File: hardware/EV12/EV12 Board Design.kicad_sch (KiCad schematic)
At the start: 132 parts, among them CN2 Conn_05x02_Female, CN3 Conn_01x06_Female, CN4 Conn_01x06_Female, CN5 Conn_02x05_Male, CN6 Conn_02x05_Male, CN7 Conn_02x05_Male, J1 Conn_01x02_Socket, J10 Conn_01x08_Socket, J2 AudioJack1, J3 Conn_01x06_Socket, J9 USB_C_Receptacle, Q1 SS8050, Q2 SS8050, SW1 TS-1037-A11B3-D2, SW3 TS-1037-A11B3-D2, SW4 SW_Push, SW5 SW_Push, SW6 SW_SPDT, U1 STM32F405RGTx, U11 ESP32-S3-WROOM-1-N8R2, U13 BM14B(0.8)-24DS-0.4V(53), U2 BQ21040DBV, U3 CH340C, U4 USBLC6-2P6, U5 M24C02-RMN6TP, U6 WM8960CGEFL/RV, U7 TPS63060, U8 STM32F072CBTx, Y1 Crystal_GND24

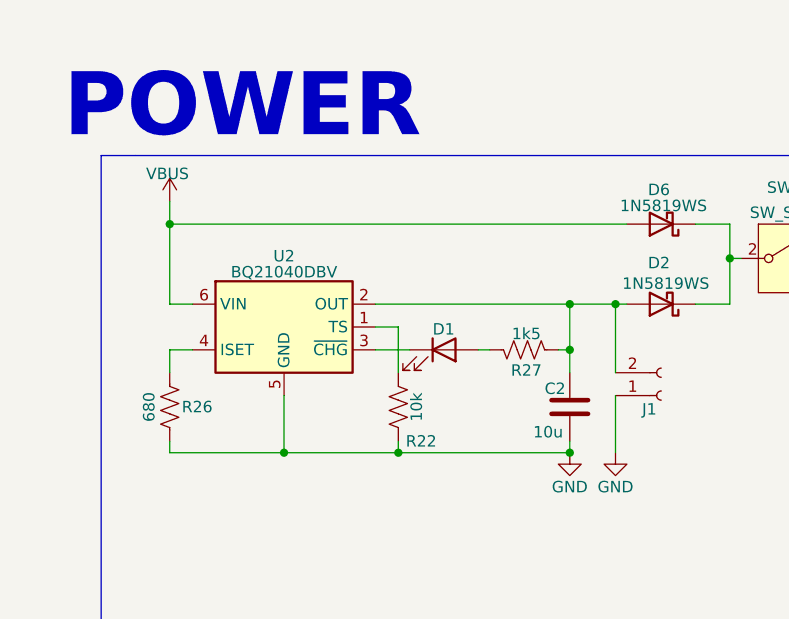
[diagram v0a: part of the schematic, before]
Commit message: Added missing capacitor to BQ21040DVR battery charger
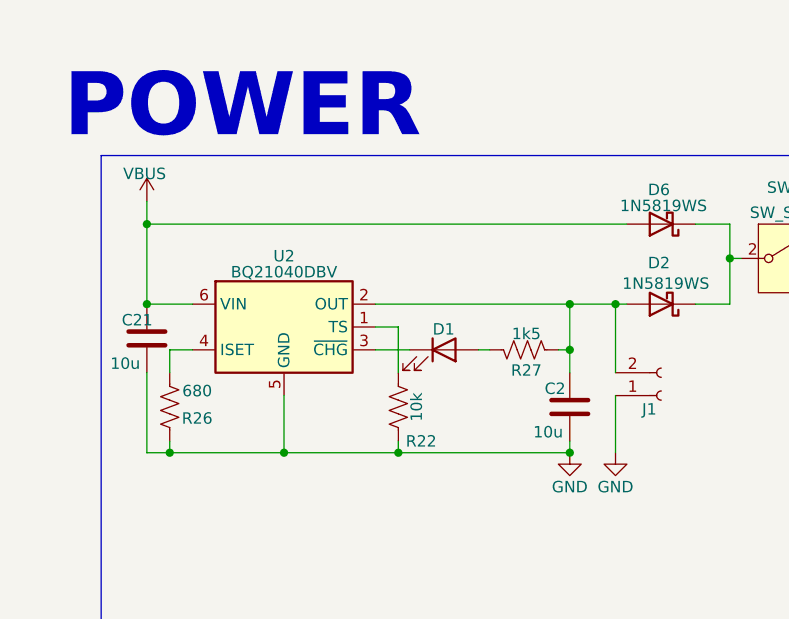
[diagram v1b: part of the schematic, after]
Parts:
- added C21: 10u, Capacitor_SMD:C_0402_1005Metric, symbol Device:C
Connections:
- net GND: now also C21.2
- net VBUS: now also C21.1
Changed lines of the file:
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@@
 	)
 	(junction
+		(at 33.02 311.15)
+		(diameter 0)
+		(color 0 0 0 0)
+	)
+	(junction
 		(at 265.43 351.79)
 		(diameter 0)
@@
 	)
 	(junction
+		(at 35.56 327.66)
+		(diameter 0)
+		(color 0 0 0 0)
+	)
+	(junction
 		(at 405.13 161.29)
 		(diameter 0)
@@
 	)
 	(junction
+		(at 33.02 302.26)
+		(diameter 0)
+		(color 0 0 0 0)
+	)
+	(junction
 		(at 196.85 351.79)
 		(diameter 0)
@@
 		(color 0 0 0 0)
 	)
-	(junction
-		(at 35.56 302.26)
-		(diameter 0)
-		(color 0 0 0 0)
-	)
 	(no_connect
 		(at 196.85 127)
@@
 		)
 	)
+	(wire
+		(pts
+			(xy 33.02 302.26) (xy 86.36 302.26)
+		)
+		(stroke
+			(width 0)
+			(type default)
+		)
+	)
 	(polyline
 		(pts
@@
 	(wire
 		(pts
+			(xy 35.56 327.66) (xy 48.26 327.66)
+		)
+		(stroke
+			(width 0)
+			(type default)
+		)
+	)
+	(wire
+		(pts
 			(xy 80.01 311.15) (xy 80.01 316.23)
 		)
@@
 	(wire
 		(pts
-			(xy 35.56 311.15) (xy 38.1 311.15)
+			(xy 33.02 311.15) (xy 38.1 311.15)
 		)
 		(stroke
@@
 	(wire
 		(pts
-			(xy 35.56 327.66) (xy 48.26 327.66)
-		)
-		(stroke
-			(width 0)
-			(type default)
-		)
-	)
-	(wire
-		(pts
 			(xy 403.86 290.83) (xy 403.86 293.37)
 		)
@@
 	(wire
 		(pts
+			(xy 33.02 327.66) (xy 35.56 327.66)
+		)
+		(stroke
+			(width 0)
+			(type default)
+		)
+	)
+	(wire
+		(pts
 			(xy 129.54 128.27) (xy 140.97 128.27)
 		)
@@
 		)
 	)
+	(wire
+		(pts
+			(xy 33.02 318.77) (xy 33.02 327.66)
+		)
+		(stroke
+			(width 0)
+			(type default)
+		)
+	)
 	(polyline
 		(pts
@@
 	(wire
 		(pts
-			(xy 35.56 302.26) (xy 35.56 311.15)
+			(xy 33.02 302.26) (xy 33.02 311.15)
 		)
 		(stroke
@@
 	(wire
 		(pts
-			(xy 35.56 302.26) (xy 86.36 302.26)
-		)
-		(stroke
-			(width 0)
-			(type default)
-		)
-	)
-	(wire
-		(pts
 			(xy 293.37 288.29) (xy 293.37 293.37)
 		)
@@
 	(wire
 		(pts
-			(xy 35.56 299.72) (xy 35.56 302.26)
+			(xy 33.02 299.72) (xy 33.02 302.26)
 		)
 		(stroke
@@
 		(dnp no)
 		(property "Reference" "R26"
-			(at 38.608 322.58 0)
+			(at 38.608 323.85 0)
 			(effects
 				(font
@@
 		)
 		(property "Value" "680"
-			(at 33.274 322.58 90)
+			(at 38.608 320.802 0)
 			(effects
 				(font
@@
 	)
 	(symbol
+		(lib_id "Device:C")
+		(at 33.02 314.96 0)
+		(unit 1)
+		(exclude_from_sim no)
+		(in_bom yes)
+		(on_board yes)
+		(dnp no)
+		(property "Reference" "C21"
+			(at 30.226 312.928 0)
+			(effects
+				(font
+					(size 1.27 1.27)
+				)
+				(justify left)
+			)
+		)
+		(property "Value" "10u"
+			(at 28.956 317.754 0)
+			(effects
+				(font
+					(size 1.27 1.27)
+				)
+				(justify left)
+			)
+		)
+		(property "Footprint" "Capacitor_SMD:C_0402_1005Metric"
+			(at 33.9852 318.77 0)
+			(effects
+				(font
+					(size 1.27 1.27)
+				)
+				(hide yes)
+			)
+		)
+		(property "Datasheet" "~"
+			(at 33.02 314.96 0)
+			(effects
+				(font
+					(size 1.27 1.27)
+				)
+				(hide yes)
+			)
+		)
+		(property "Description" "Unpolarized capacitor"
+			(at 33.02 314.96 0)
+			(effects
+				(font
+					(size 1.27 1.27)
+				)
+				(hide yes)
+			)
+		)
+		(property "JLCPCB Part #" "C307415"
+			(at 33.02 314.96 0)
+			(effects
+				(font
+					(size 1.27 1.27)
+				)
+				(hide yes)
+			)
+		)
+		(pin "1"
+		)
+		(pin "2"
+		)
+		(instances
+			(project "EV12 Board Design"
+				(path "/bd865368-262b-4f76-b7a6-1673c2cb0f8c"
+					(reference "C21")
+					(unit 1)
+				)
+			)
+		)
+	)
+	(symbol
 		(lib_id "Device:R_US")
 		(at 109.22 331.47 180)
@@
 	(symbol
 		(lib_id "power:VBUS")
-		(at 35.56 299.72 0)
+		(at 33.02 299.72 0)
 		(unit 1)
 		(exclude_from_sim no)
@@
 		(dnp no)
 		(property "Reference" "#PWR03"
-			(at 35.56 303.53 0)
+			(at 33.02 303.53 0)
 			(effects
 				(font
@@
 		)
 		(property "Value" "VBUS"
-			(at 35.306 296.672 0)
+			(at 32.766 296.672 0)
 			(effects
 				(font
@@
 		)
 		(property "Footprint" ""
-			(at 35.56 299.72 0)
+			(at 33.02 299.72 0)
 			(effects
 				(font
@@
 		)
 		(property "Datasheet" ""
-			(at 35.56 299.72 0)
+			(at 33.02 299.72 0)
 			(effects
 				(font
@@
 		)
 		(property "Description" "Power symbol creates a global label with name \"VBUS\""
-			(at 35.56 299.72 0)
+			(at 33.02 299.72 0)
 			(effects
 				(font

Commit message: Moved keyboard conn, eeprom, and battery connector. Added diodes
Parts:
- added D10, D11, D12, D13, D14, D15, D8, D9: 1N5819WS, Diode_SMD:D_SOD-323, symbol Device:D_Schottky
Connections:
- net NET_BOOT: now also D12.1 (K); no longer U8.41 (PB5)
- net NET_DTR: now also D11.2 (A); no longer Q1.2 (E), R44.1
- net NET_NRST: now also D13.1 (K); no longer U8.40 (PB4)
- net NET_RTS: now also D10.2 (A); no longer Q2.2 (E), R43.1
- net UI_BOOT0: now also D14.1 (K), D9.1 (K); no longer CN4.5 (Pin_5), U8.39 (PB3)
- net UI_NRST: now also D15.1 (K), D8.1 (K); no longer CN4.4 (Pin_4), U8.38 (PA15)
- new net: D12.2 (A), U8.38 (PA15)
- new net: CN4.4 (Pin_4), D15.2 (A)
- new net: CN4.5 (Pin_5), D14.2 (A)
- new net: D13.2 (A), U8.39 (PB3)
- new net: D8.2 (A), U8.40 (PB4)
- new net: D9.2 (A), U8.41 (PB5)
- new net: D11.1 (K), Q1.2 (E), R44.1
- new net: D10.1 (K), Q2.2 (E), R43.1
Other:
- note added: "UI ST-LINK - 2MM R"
- note removed: "MAIN ST-LINK - 2MM R"
- moved on the sheet: CN4, Q1, Q2, R4, R43, R44

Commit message: Removed diodes and auto reset circuit
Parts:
- removed D10, D11, D12, D13, D14, D15, D8, D9: 1N5819WS, Diode_SMD:D_SOD-323, symbol Device:D_Schottky
- removed Q1, Q2: SS8050, Package_TO_SOT_SMD:SOT-23, symbol Transistor_BJT:SS8050
- removed R43, R44: 10k, Resistor_SMD:R_0402_1005Metric, symbol Device:R_US
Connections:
- net NET_DTR is gone; now on net NET_BOOT: J3.2 (Pin_2)
- net NET_RTS is gone; now on net NET_NRST: J3.5 (Pin_5)
- net NET_BOOT: now also U8.41 (PB5)
- net NET_NRST: now also U8.40 (PB4)
- net UI_BOOT0: now also CN4.5 (Pin_5), U8.38 (PA15)
- net UI_NRST: now also CN4.4 (Pin_4), U8.39 (PB3)
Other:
- note removed: "NET AUTO RESET"

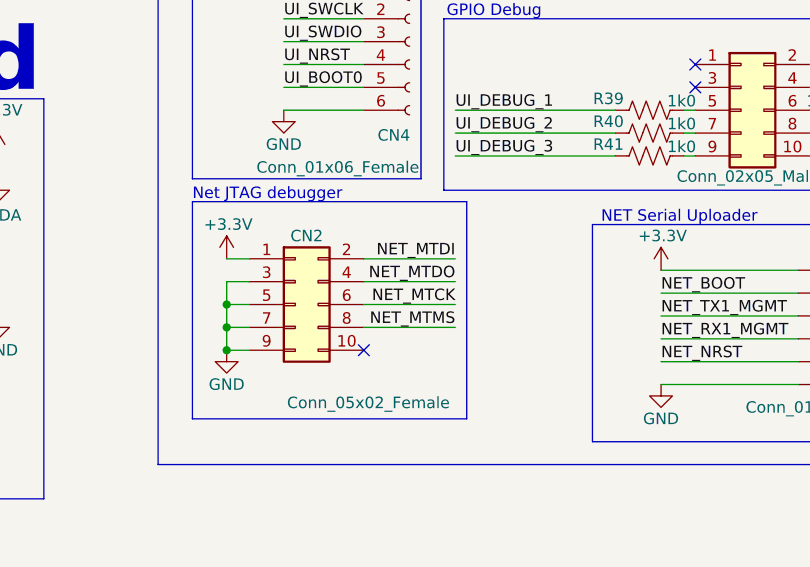
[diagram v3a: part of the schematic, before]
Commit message: Added some design rules, updated track widths to be between 5 to 15mils except for long power lines
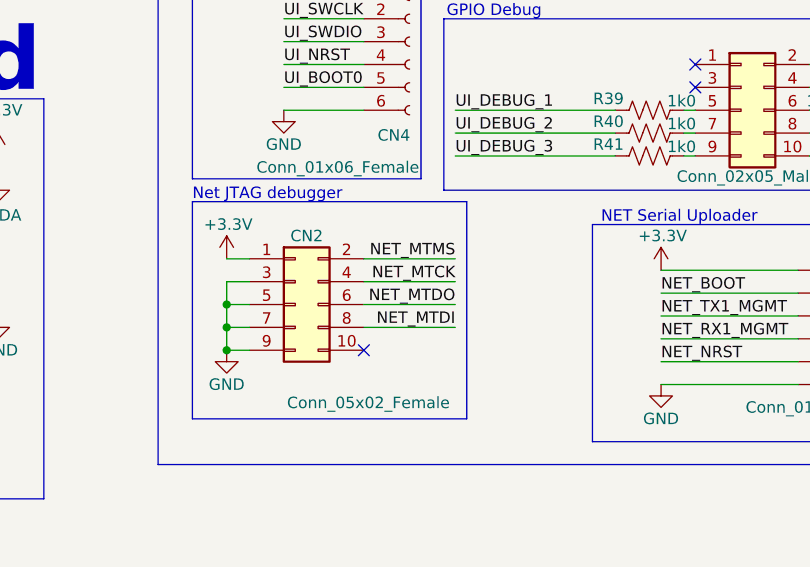
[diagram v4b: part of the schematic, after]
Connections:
- net NET_MTCK: now also CN2.4 (Pin_4); no longer CN2.6 (Pin_6)
- net NET_MTDI: now also CN2.8 (Pin_8); no longer CN2.2 (Pin_2)
- net NET_MTDO: now also CN2.6 (Pin_6); no longer CN2.4 (Pin_4)
- net NET_MTMS: now also CN2.2 (Pin_2); no longer CN2.8 (Pin_8)
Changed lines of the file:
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@@
+		)
+	)
+	(label "NET_MTDO"
+		(at 429.26 288.29 180)
+		(fields_autoplaced yes)
+		(effects
+			(font
+				(size 1.27 1.27)
+			)
+			(justify right bottom)
 		)
 	)
@@
 		)
 	)
-	(label "NET_MTDI"
-		(at 429.26 283.21 180)
-		(fields_autoplaced yes)
-		(effects
-			(font
-				(size 1.27 1.27)
-			)
-			(justify right bottom)
-		)
-	)
 	(label "NET_NRST"
 		(at 181.61 96.52 0)
@@
 		)
 	)
-	(label "NET_MTDO"
-		(at 429.26 285.75 180)
-		(fields_autoplaced yes)
-		(effects
-			(font
-				(size 1.27 1.27)
-			)
-			(justify right bottom)
-		)
-	)
 	(label "DISP_RST"
 		(at 314.96 223.52 0)
@@
 		)
 	)
-	(label "NET_MTCK"
-		(at 429.26 288.29 180)
-		(fields_autoplaced yes)
-		(effects
-			(font
-				(size 1.27 1.27)
-			)
-			(justify right bottom)
-		)
-	)
 	(label "NET_RX1_MGMT"
 		(at 452.12 292.1 0)
@@
 		)
 	)
+	(label "NET_MTDI"
+		(at 429.26 290.83 180)
+		(fields_autoplaced yes)
+		(effects
+			(font
+				(size 1.27 1.27)
+			)
+			(justify right bottom)
+		)
+	)
 	(label "UI_SCL"
 		(at 214.63 214.63 0)
@@
 		)
 	)
-	(label "NET_MTMS"
-		(at 429.26 290.83 180)
-		(fields_autoplaced yes)
-		(effects
-			(font
-				(size 1.27 1.27)
-			)
-			(justify right bottom)
-		)
-	)
 	(label "UI_SDA"
 		(at 287.02 283.21 0)
@@
 		)
 	)
+	(label "NET_MTCK"
+		(at 429.26 285.75 180)
+		(fields_autoplaced yes)
+		(effects
+			(font
+				(size 1.27 1.27)
+			)
+			(justify right bottom)
+		)
+	)
 	(label "I2S_DACDAT"
 		(at 485.14 247.65 180)
@@
 		(fields_autoplaced yes)
 		(effects
+			(font
+				(size 1.27 1.27)
+			)
+			(justify right bottom)
+		)
+	)
+	(label "NET_MTMS"
+		(at 429.26 283.21 180)
+		(fields_autoplaced yes)
+		(effects

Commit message: Finish ev12 design
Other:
- company: CISCO SYSTEMS -> CISCO SYSTEMS INC
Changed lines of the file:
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@@
 		(title "EV12 FINN BERG & BRETT REGNIER")
 		(date "2024/07/19")
-		(company "CISCO SYSTEMS")
+		(company "CISCO SYSTEMS INC")
 	)
 	(junction

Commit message: Added missing jlcpcb part number
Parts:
- R42: JLCPCB Part # (none) -> C111027
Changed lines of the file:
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@@
 			)
 		)
-		(property "JLCPCB Part #" ""
+		(property "JLCPCB Part #" "C111027"
 			(at 116.84 322.58 0)
 			(effects

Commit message: Replaced side buttons, switched Cap, switched to new connectors
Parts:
- SW1, SW3: footprint Hactar_Footprints:KEY-SMD_2P-L7.1-W10.6-P4.00-LS9.0 -> Hactar_Footprints:SW-SMD_L7.5-W8.0-P4.50_TS-1045-A13B3-D2

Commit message: Updated Version with fixes
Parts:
- removed SW3: TS-1037-A11B3-D2, Hactar_Footprints:SW-SMD_L7.5-W8.0-P4.50_TS-1045-A13B3-D2, symbol Switch:SW_Push
- added SW2: SW_Push, Hactar_Footprints:SW-SMD_L7.5-W8.0-P4.50_TS-1045-A13B3-D2, symbol Switch:SW_Push
- C37, C40, C42: JLCPCB Part # C495959 -> C85866
- CN2, CN5, CN6, CN7: JLCPCB Part # C2962219 -> C2962222
- SW1: value TS-1037-A11B3-D2 -> SW_Push; JLCPCB Part # C499331 -> C557898; JLCPCB Position Offset 0,-0.635 -> (none); LCSC Part C499331 -> (none)
- U2: JLCPCB Part # (none) -> C202311
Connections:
- net GND: now also SW2.2
- net PTT_AI_BTN: now also SW2.1
